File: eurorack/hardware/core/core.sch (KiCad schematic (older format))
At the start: 19 parts, among them J1 ConnNW, J2 ConnSW, J3 ConnNE, J4 ConnSE, J5 Power, J6 SWD, SW1 Reset, SW2 Boot0, U1 STM32F427VGT6, U2 TLV320AIC23BPW, U3 LM1117F-3.3, Y1 Crystal

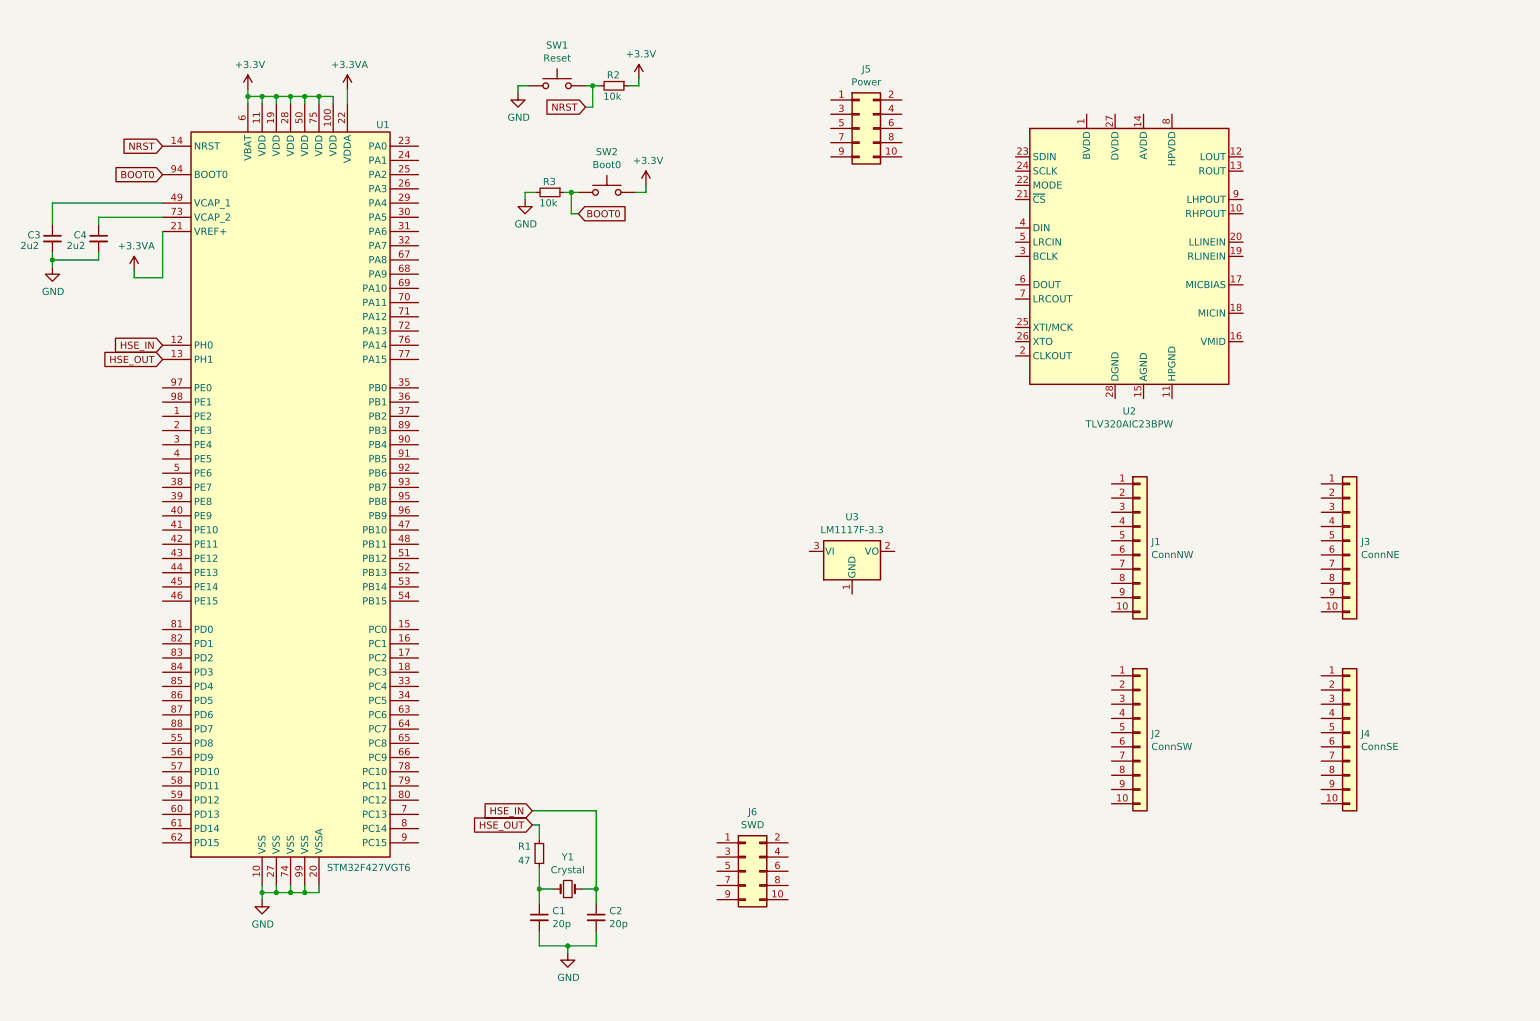
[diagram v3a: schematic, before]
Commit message: Isoolate 3.3v power from MCU
Signed-off-by: Petr Horacek <hrck@protonmail.com>
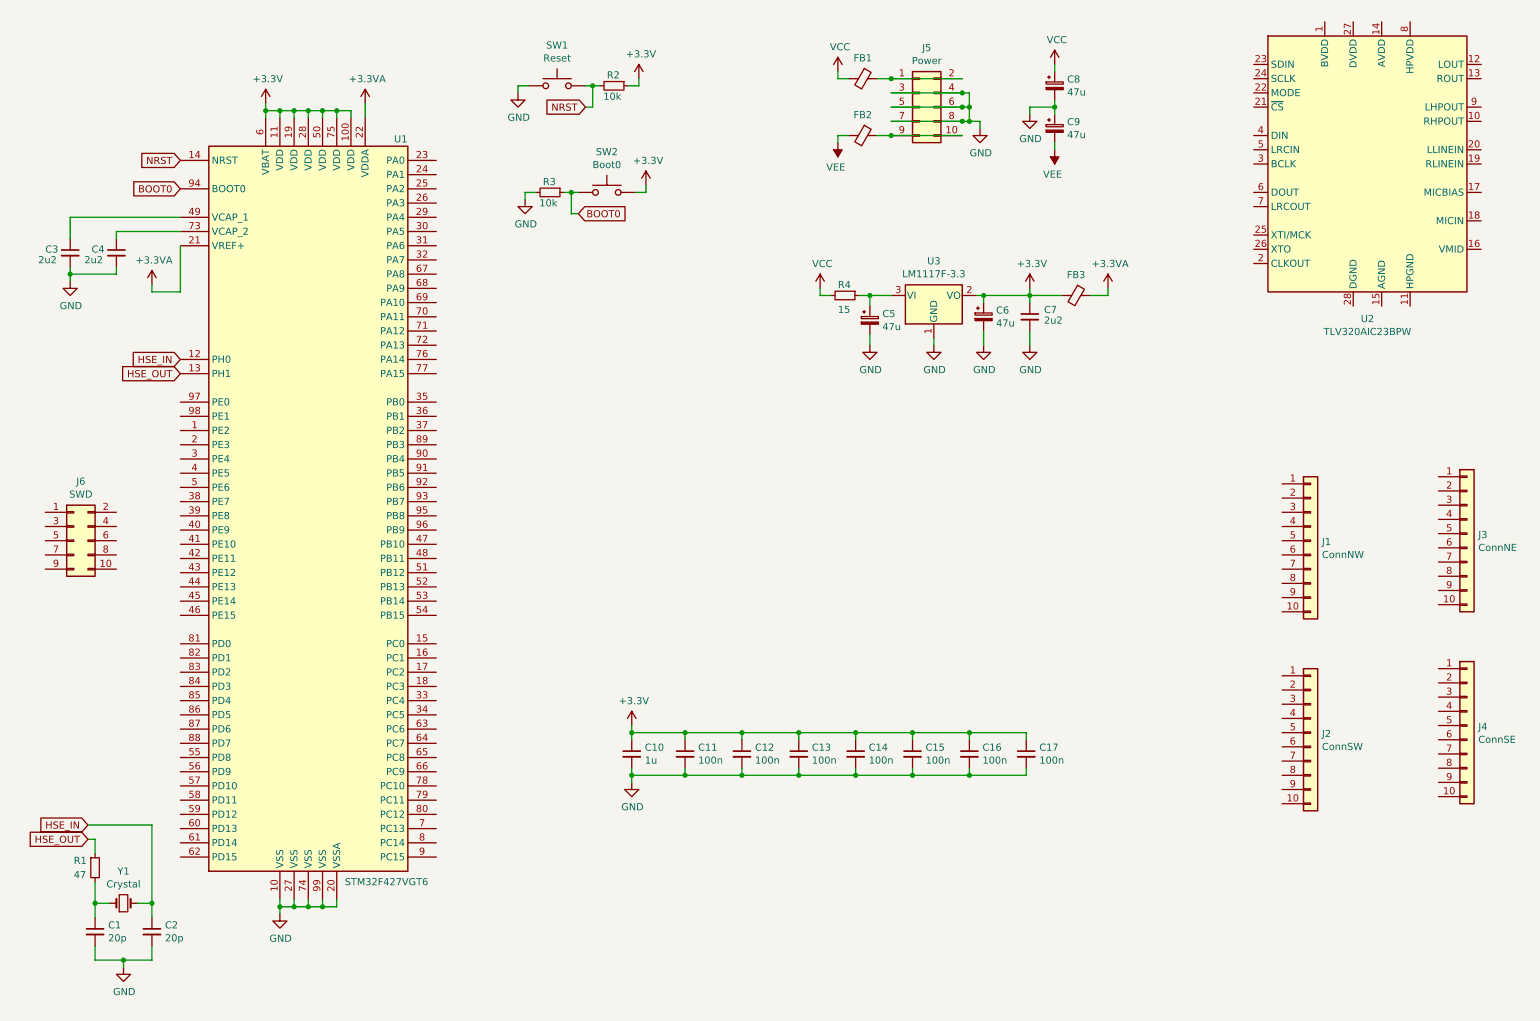
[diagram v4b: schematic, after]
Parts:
- added C10: 1u, Capacitor_SMD:C_0402_1005Metric, symbol Device:C_Small
- added C11, C12, C13, C14, C15, C16, C17: 100n, Capacitor_SMD:C_0402_1005Metric, symbol Device:C_Small
- added C5, C6, C8, C9: 47u, Capacitor_Tantalum_SMD:CP_EIA-3216-18_Kemet-A, symbol Device:CP_Small
- added C7: 2u2, Capacitor_SMD:C_0603_1608Metric, symbol Device:C_Small
- added FB1, FB2, FB3: Ferrite_Bead_Small, Inductor_SMD:L_0805_2012Metric, symbol Device:Ferrite_Bead_Small
- added R4: 15, Resistor_SMD:R_0402_1005Metric, symbol Device:R_Small
- J6: footprint Connector_PinHeader_2.54mm:PinHeader_2x05_P2.54mm_Vertical -> Connector_PinHeader_1.27mm:PinHeader_2x05_P1.27mm_Vertical
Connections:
- net +3.3VA: now also FB3.1
- net +3V3: now also U3.2 (VO), C10.1, C11.1, C12.1, C13.1, C14.1, C15.1, C16.1, C17.1, C6.1, C7.1, FB3.2
- net GND: now also J5.3 (Pin_3), J5.4 (Pin_4), J5.5 (Pin_5), J5.6 (Pin_6), J5.7 (Pin_7), J5.8 (Pin_8), U3.1 (GND), C10.2, C11.2, C12.2, C13.2, C14.2, C15.2, C16.2, C17.2, C5.2, C6.2, C7.2, C8.2, C9.1
- net at U3.3 (VI): now also C5.1, R4.1
- net at J5.1 (Pin_1): now also J5.2 (Pin_2), FB1.1
- net at J5.10 (Pin_10): now also J5.9 (Pin_9), FB2.1
- new net VCC: C8.1, FB1.2, R4.2
- new net VEE: C9.2, FB2.2
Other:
- moved on the sheet: C1, C2, C3, C4, J1, J2, J3, J4, J5, J6, R1, U1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

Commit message: Add decoupling capacitors
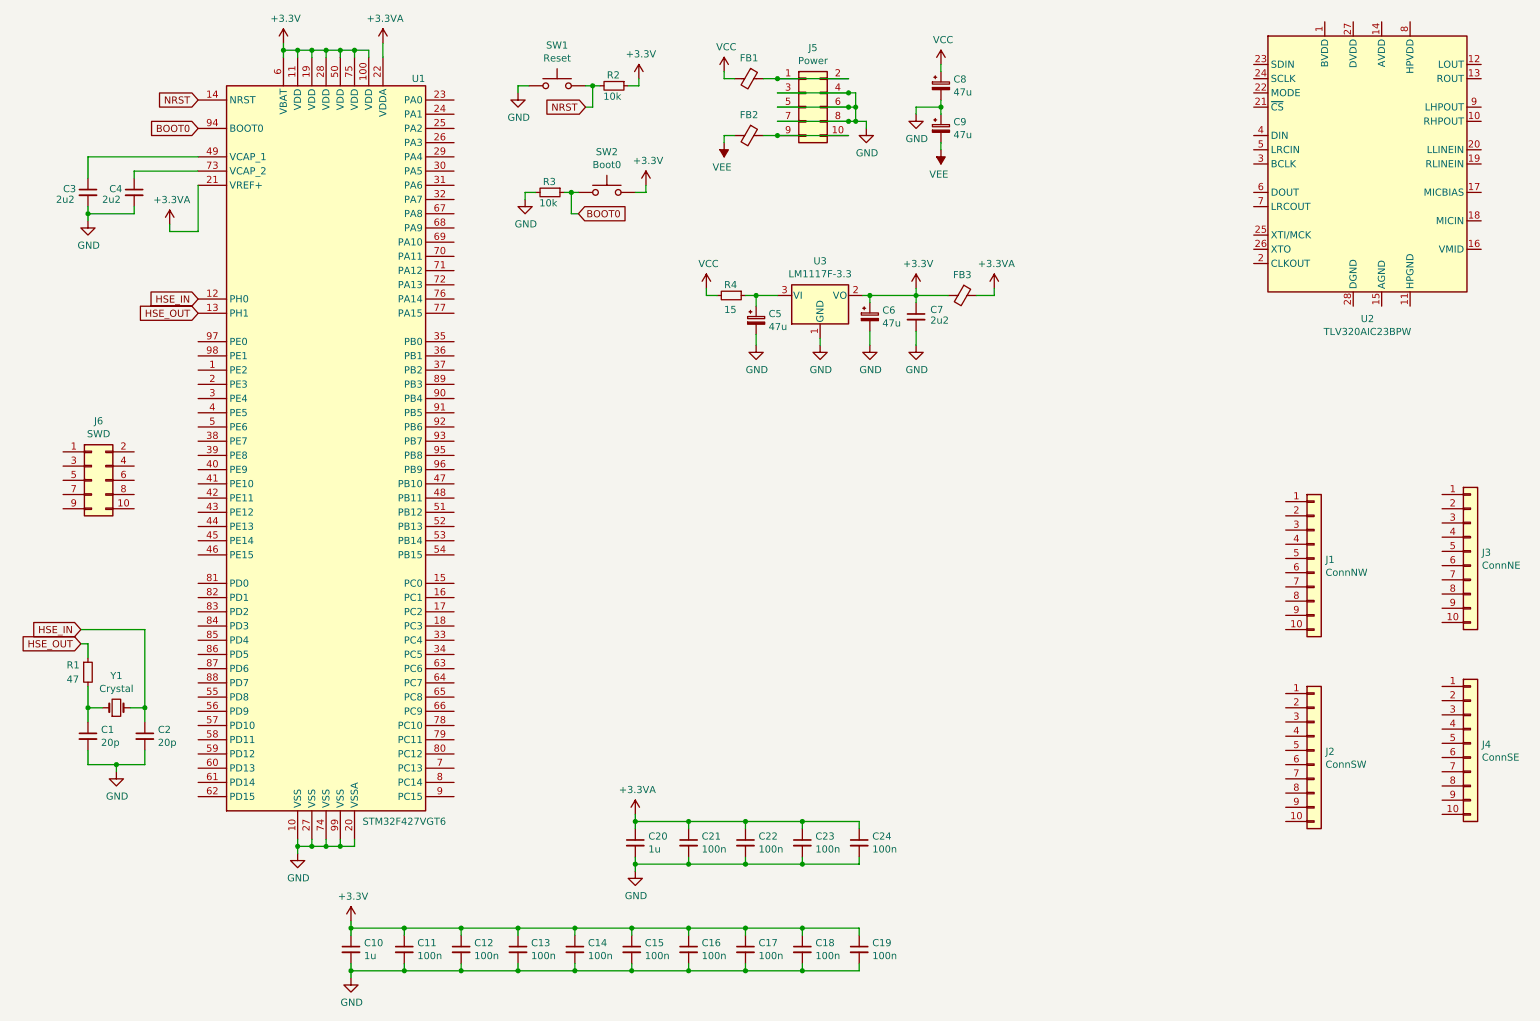
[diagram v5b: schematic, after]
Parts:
- added C18, C19, C21, C22, C23, C24: 100n, Capacitor_SMD:C_0402_1005Metric, symbol Device:C_Small
- added C20: 1u, Capacitor_SMD:C_0402_1005Metric, symbol Device:C_Small
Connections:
- net +3.3VA: now also C20.1, C21.1, C22.1, C23.1, C24.1
- net +3V3: now also C18.1, C19.1
- net GND: now also C18.2, C19.2, C20.2, C21.2, C22.2, C23.2, C24.2
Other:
- moved on the sheet: C1, C10, C11, C12, C13, C14, C15, C16, C17, C2, C3, C4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

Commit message: Fit the PCB within 2 HP
Signed-off-by: Petr Horacek <hrck@protonmail.com>
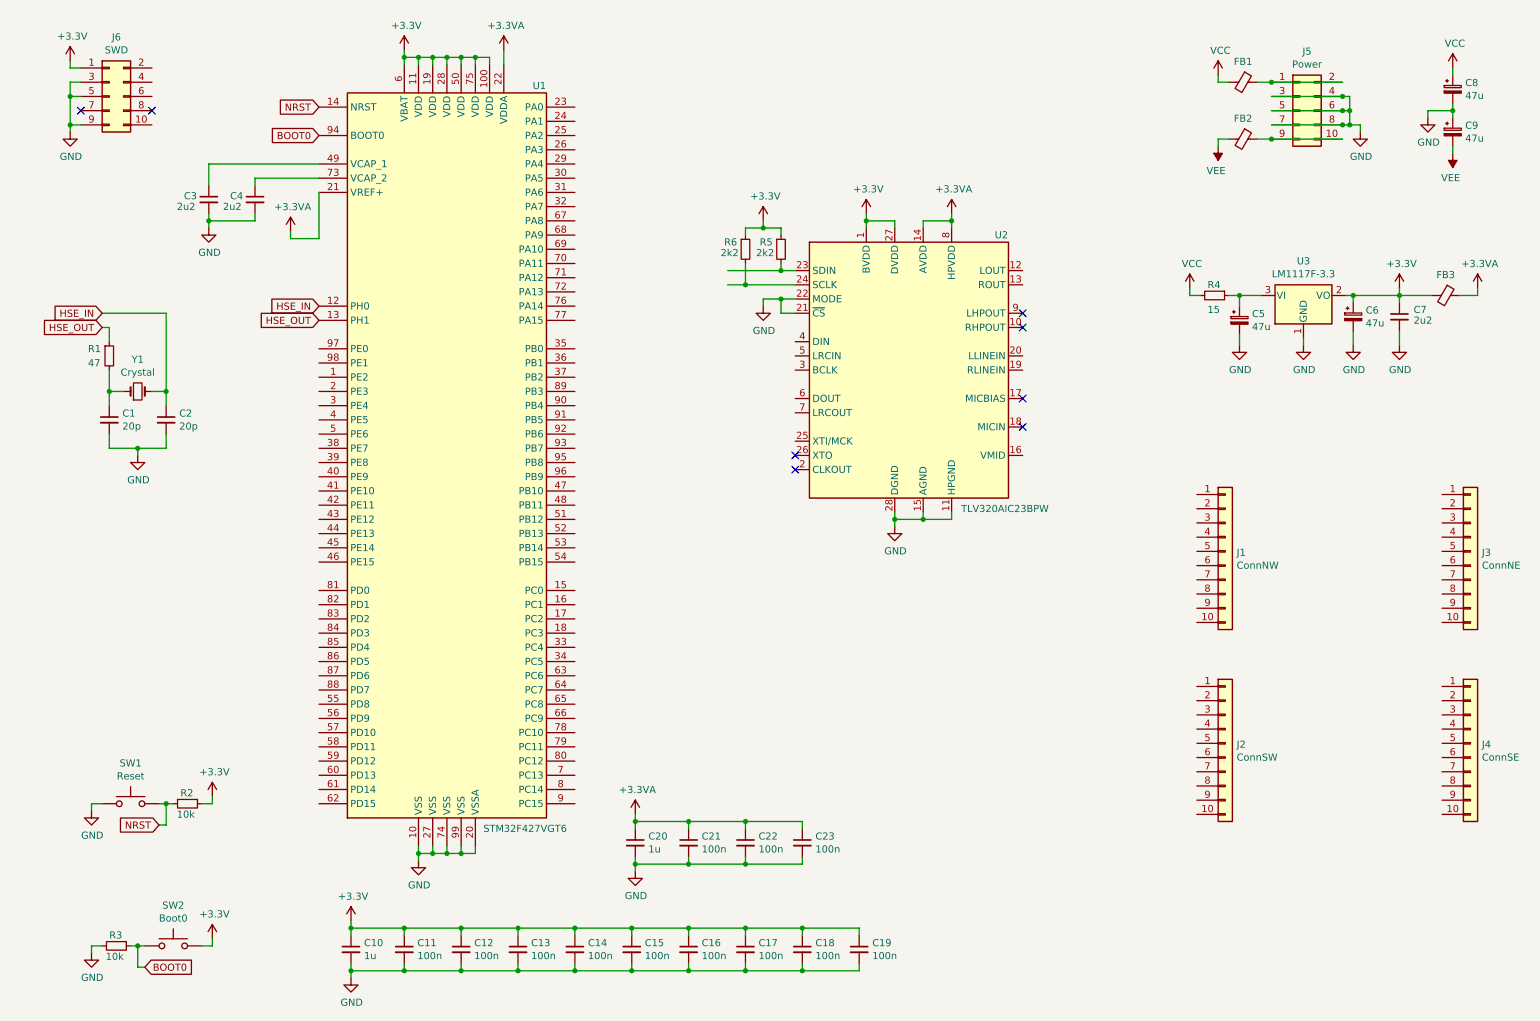
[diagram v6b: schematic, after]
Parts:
- removed C24: 100n, Capacitor_SMD:C_0402_1005Metric, symbol Device:C_Small
- added R5, R6: 2k2, Resistor_SMD:R_0402_1005Metric, symbol Device:R_Small
- R4: footprint Resistor_SMD:R_0402_1005Metric -> Resistor_SMD:R_0603_1608Metric
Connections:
- net +3.3VA: now also U2.14 (AVDD), U2.8 (HPVDD)
- net +3V3: now also J6.1 (Pin_1), U2.1 (BVDD), U2.27 (DVDD), R5.1, R6.1
- net GND: now also J6.3 (Pin_3), J6.5 (Pin_5), J6.9 (Pin_9), U2.11 (HPGND), U2.15 (AGND), U2.21 (~CS~), U2.22 (MODE), U2.28 (DGND)
- net at U2.23 (SDIN): now also R5.2
- net at U2.24 (SCLK): now also R6.2
- no-connect marks 0 -> 8
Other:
- moved on the sheet: C1, C2, C3, C4, C5, C6, C7, C8, C9, FB1, FB2, FB3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

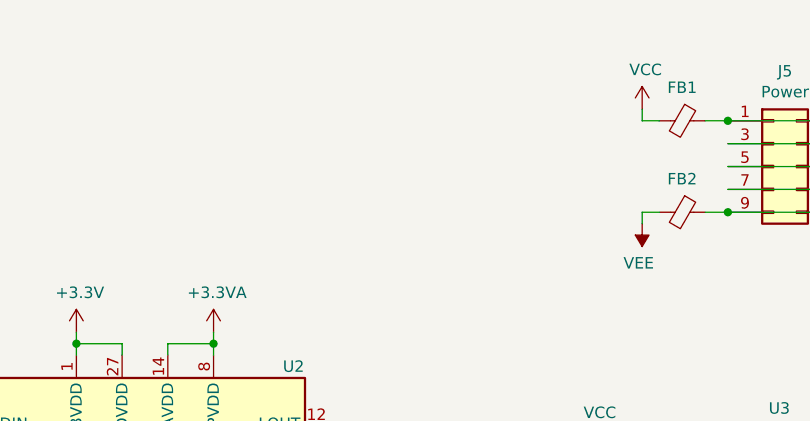
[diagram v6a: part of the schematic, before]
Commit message: Add -10v reference voltage
Signed-off-by: Petr Horacek <hrck@protonmail.com>
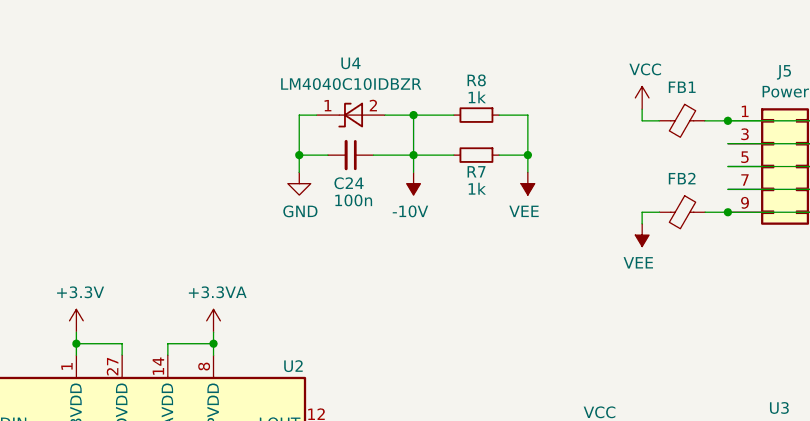
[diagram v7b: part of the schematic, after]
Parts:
- added C24: 100n, Capacitor_SMD:C_0805_2012Metric, symbol Device:C_Small
- added R7, R8: 1k, Resistor_SMD:R_0805_2012Metric, symbol Device:R_Small
- added U4: LM4040C10IDBZR, Package_TO_SOT_SMD:SOT-23, symbol Reference_Voltage:LM4040DBZ-10
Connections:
- net GND: now also C24.2, U4.1 (K)
- net VEE: now also R7.1, R8.1
- new net -10V: C24.1, R7.2, R8.2, U4.2 (A)
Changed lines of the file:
@@
 	1    0    0    -1
 $EndComp
+$Comp
+L Reference_Voltage:LM4040DBZ-10 U4
+U 1 1 615D2ED0
+P 7700 1050
+F 0 "U4" H 7700 825 50  0000 C CNN
+F 1 "LM4040C10IDBZR" H 7700 916 50  0000 C CNN
+F 2 "Package_TO_SOT_SMD:SOT-23" H 7700 850 50  0001 C CIN
+F 3 "http://www.ti.com/lit/ds/symlink/lm4040-n.pdf" H 7700 1050 50  0001 C CIN
+	1    7700 1050
+	-1   0    0    1
+$EndComp
+$Comp
+L Device:C_Small C24
+U 1 1 615D754F
+P 7700 1225
+F 0 "C24" V 7825 1150 50  0000 L CNN
+F 1 "100n" V 7900 1150 50  0000 L CNN
+F 2 "Capacitor_SMD:C_0805_2012Metric" H 7700 1225 50  0001 C CNN
+F 3 "~" H 7700 1225 50  0001 C CNN
+	1    7700 1225
+	0    1    1    0
+$EndComp
+$Comp
+L power:-10V #PWR?
+U 1 1 615DBA60
+P 7975 1300
+F 0 "#PWR?" H 7975 1400 50  0001 C CNN
+F 1 "-10V" H 7990 1473 50  0000 C CNN
+F 2 "" H 7975 1300 50  0001 C CNN
+F 3 "" H 7975 1300 50  0001 C CNN
+	1    7975 1300
+	-1   0    0    1
+$EndComp
+$Comp
+L Device:R_Small R8
+U 1 1 615D2074
+P 8250 1050
+F 0 "R8" V 8100 1050 50  0000 C CNN
+F 1 "1k" V 8175 1050 50  0000 C CNN
+F 2 "Resistor_SMD:R_0805_2012Metric" H 8250 1050 50  0001 C CNN
+F 3 "~" H 8250 1050 50  0001 C CNN
+	1    8250 1050
+	0    1    1    0
+$EndComp
+$Comp
+L Device:R_Small R7
+U 1 1 615D0D2B
+P 8250 1225
+F 0 "R7" V 8325 1225 50  0000 C CNN
+F 1 "1k" V 8400 1225 50  0000 C CNN
+F 2 "Resistor_SMD:R_0805_2012Metric" H 8250 1225 50  0001 C CNN
+F 3 "~" H 8250 1225 50  0001 C CNN
+	1    8250 1225
+	0    1    1    0
+$EndComp
+$Comp
+L power:GND #PWR?
+U 1 1 6167B96E
+P 7475 1300
+F 0 "#PWR?" H 7475 1050 50  0001 C CNN
+F 1 "GND" H 7480 1127 50  0000 C CNN
+F 2 "" H 7475 1300 50  0001 C CNN
+F 3 "" H 7475 1300 50  0001 C CNN
+	1    7475 1300
+	1    0    0    -1
+$EndComp
+$Comp
+L power:VEE #PWR?
+U 1 1 6167C276
+P 8475 1300
+F 0 "#PWR?" H 8475 1150 50  0001 C CNN
+F 1 "VEE" H 8490 1473 50  0000 C CNN
+F 2 "" H 8475 1300 50  0001 C CNN
+F 3 "" H 8475 1300 50  0001 C CNN
+	1    8475 1300
+	-1   0    0    1
+$EndComp
+Wire Wire Line
+	7475 1300 7475 1225
+Wire Wire Line
+	7475 1225 7600 1225
+Wire Wire Line
+	7550 1050 7475 1050
+Wire Wire Line
+	7475 1050 7475 1225
+Connection ~ 7475 1225
+Wire Wire Line
+	7850 1050 7975 1050
+Wire Wire Line
+	8150 1225 7975 1225
+Wire Wire Line
+	7975 1300 7975 1225
+Connection ~ 7975 1225
+Wire Wire Line
+	7975 1225 7800 1225
+Wire Wire Line
+	7975 1225 7975 1050
+Connection ~ 7975 1050
+Wire Wire Line
+	7975 1050 8150 1050
+Wire Wire Line
+	8350 1225 8475 1225
+Wire Wire Line
+	8475 1225 8475 1300
+Wire Wire Line
+	8475 1225 8475 1050
+Wire Wire Line
+	8475 1050 8350 1050
+Connection ~ 8475 1225
 $EndSCHEMATC
